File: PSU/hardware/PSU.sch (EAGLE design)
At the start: 203 parts, among them J1 SWD, J2 UART, Q1 PMOS-DPAK, Q10 PMOS-SOT23, Q11 NPN, Q12 PMOS-SOT23, Q2 PMOS-SOT23, Q3 NPN, Q4 PMOS-SOT23, Q5 NMOS-SOT23, Q6 PMOS-DPAK, Q7 PMOS-SOT23, Q8 NMOS-SOT23, Q9 PMOS-DPAK, U1 LM2576, U10 4069, U11 LTV-247, U12 74HC08, U13 STM8S003K3T6C, U14 74HC08, U15 4051, U16 358, U17 358, U18 74HC32, U2 MT3608, U3 7805, U4 324, U5 MC34063, U6 MT3608, U7 LM2576, U8 MC34063, U9 TP4056

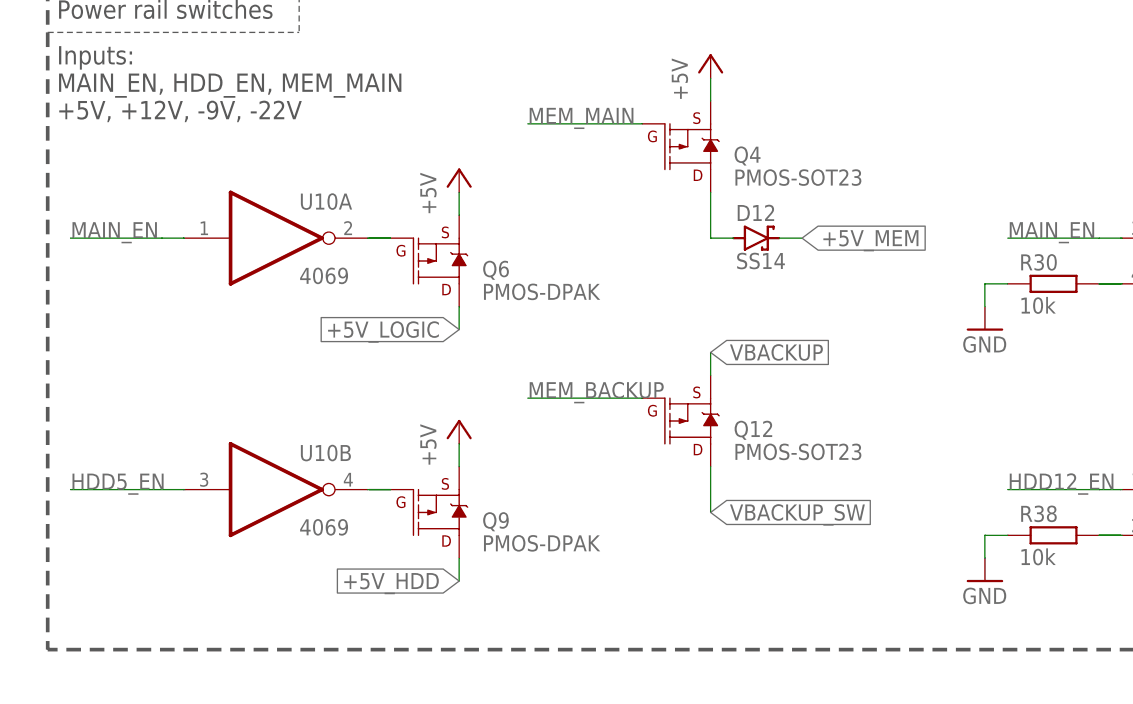
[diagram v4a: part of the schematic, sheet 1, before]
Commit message: [HW/PSU] Fix backup regulator enabling logic level
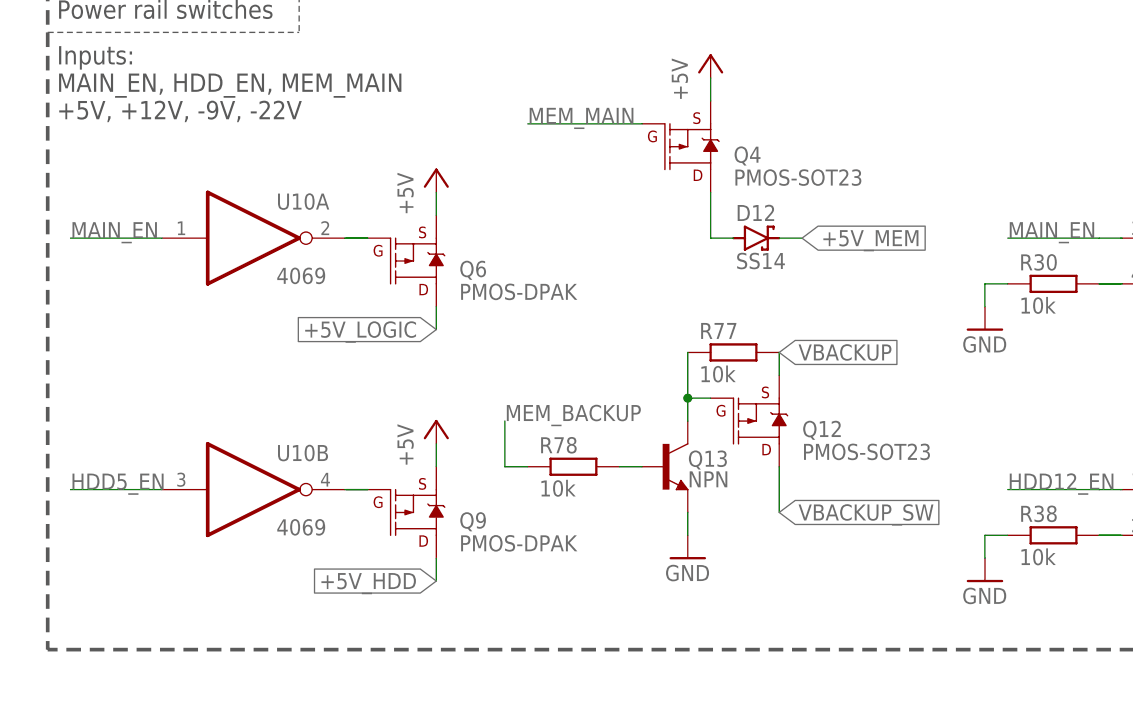
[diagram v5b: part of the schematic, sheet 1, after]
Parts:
- added Q13: NPN, SparkFun-DiscreteSemi:TRANS_NPN-MMBT2222AL
- added R77, R78: 10k, rcl:R-EU_R0805
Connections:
- new net VBACKUP_SW_B: Q13.B, R78.2
- new net VBACKUP_SW_G: Q12.G, Q13.C, R77.1
- net GND: now also Q13.E
- net MEM_BACKUP: now also R78.1; no longer Q12.G
- net VBACKUP: now also R77.2
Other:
- moved on the sheet: Q12, Q6, Q9, U10A, U10B

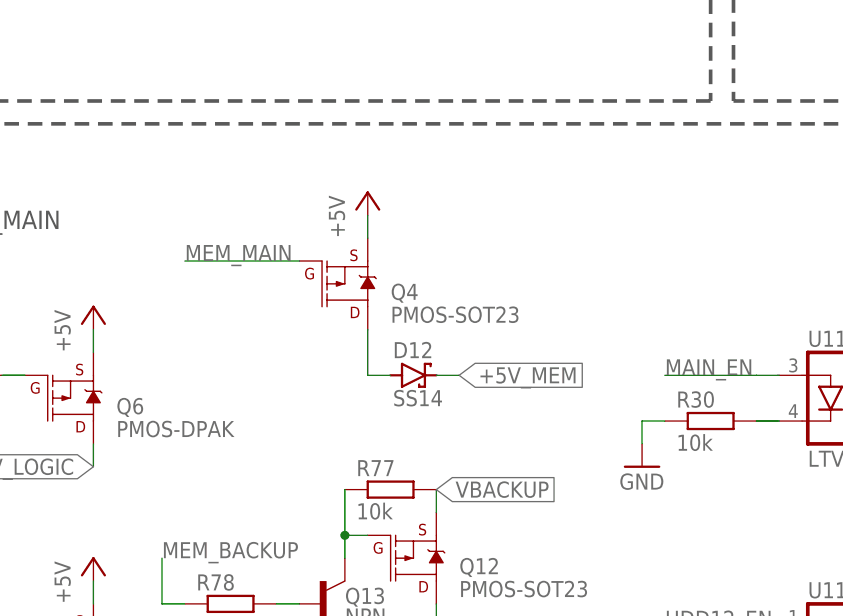
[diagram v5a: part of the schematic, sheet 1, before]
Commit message: [HW/PSU] Fix +5V_MEM enabling logic level
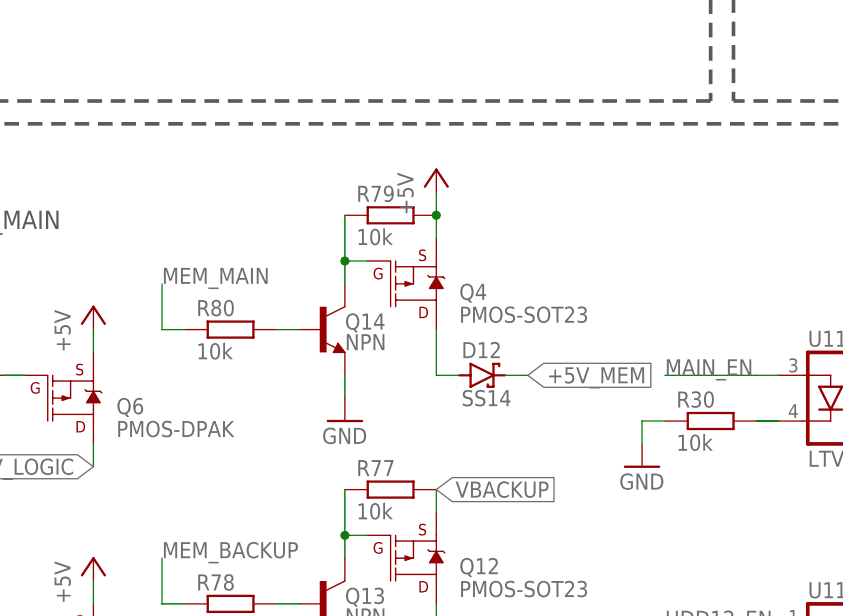
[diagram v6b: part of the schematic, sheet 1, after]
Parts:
- added Q14: NPN, SparkFun-DiscreteSemi:TRANS_NPN-MMBT2222AL
- added R79, R80: 10k, rcl:R-EU_R0805
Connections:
- new net +5VMEM_B: Q14.B, R80.2
- new net +5VMEM_G: Q14.C, Q4.G, R79.1
- net +5V: now also R79.2
- net GND: now also Q14.E
- net MEM_MAIN: now also R80.1; no longer Q4.G
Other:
- moved on the sheet: D12, Q4
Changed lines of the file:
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@@
 <part name="R77" library="rcl" library_urn="urn:adsk.eagle:library:334" deviceset="R-EU_" device="R0805" package3d_urn="urn:adsk.eagle:package:23553/2" value="10k"/>
 <part name="R78" library="rcl" library_urn="urn:adsk.eagle:library:334" deviceset="R-EU_" device="R0805" package3d_urn="urn:adsk.eagle:package:23553/2" value="10k"/>
+<part name="Q14" library="SparkFun-DiscreteSemi" deviceset="TRANS_NPN" device="-MMBT2222AL" value="NPN"/>
+<part name="R80" library="rcl" library_urn="urn:adsk.eagle:library:334" deviceset="R-EU_" device="R0805" package3d_urn="urn:adsk.eagle:package:23553/2" value="10k"/>
+<part name="R79" library="rcl" library_urn="urn:adsk.eagle:library:334" deviceset="R-EU_" device="R0805" package3d_urn="urn:adsk.eagle:package:23553/2" value="10k"/>
+<part name="GND2" library="supply1" library_urn="urn:adsk.eagle:library:371" deviceset="GND" device=""/>
 </parts>
 <sheets>
@@
 <attribute name="VALUE" x="315.722" y="90.17" size="1.778" layer="96" rot="R90"/>
 </instance>
-<instance part="P+22" gate="1" x="81.28" y="73.66" smashed="yes">
-<attribute name="VALUE" x="78.74" y="68.58" size="1.778" layer="96" rot="R90"/>
-</instance>
-<instance part="Q4" gate="G$1" x="78.74" y="63.5" smashed="yes" rot="MR180">
-<attribute name="NAME" x="83.82" y="63.5" size="1.778" layer="95" font="vector" rot="MR180"/>
-<attribute name="VALUE" x="83.82" y="60.96" size="1.778" layer="96" font="vector" rot="MR180"/>
-</instance>
-<instance part="D12" gate="G$1" x="86.36" y="53.34" smashed="yes">
-<attribute name="NAME" x="84.074" y="55.245" size="1.778" layer="95"/>
-<attribute name="VALUE" x="84.074" y="49.911" size="1.778" layer="96"/>
+<instance part="P+22" gate="1" x="88.9" y="76.2" smashed="yes">
+<attribute name="VALUE" x="86.36" y="71.12" size="1.778" layer="96" rot="R90"/>
+</instance>
+<instance part="Q4" gate="G$1" x="86.36" y="63.5" smashed="yes" rot="MR180">
+<attribute name="NAME" x="91.44" y="63.5" size="1.778" layer="95" font="vector" rot="MR180"/>
+<attribute name="VALUE" x="91.44" y="60.96" size="1.778" layer="96" font="vector" rot="MR180"/>
+</instance>
+<instance part="D12" gate="G$1" x="93.98" y="53.34" smashed="yes">
+<attribute name="NAME" x="91.694" y="55.245" size="1.778" layer="95"/>
+<attribute name="VALUE" x="91.694" y="49.911" size="1.778" layer="96"/>
 </instance>
 <instance part="Q1" gate="G$1" x="152.4" y="231.14" smashed="yes">
@@
 <attribute name="NAME" x="62.23" y="29.4386" size="1.778" layer="95"/>
 <attribute name="VALUE" x="62.23" y="24.638" size="1.778" layer="96"/>
+</instance>
+<instance part="Q14" gate="G$1" x="76.2" y="58.42" smashed="yes">
+<attribute name="NAME" x="78.74" y="58.42" size="1.778" layer="95" font="vector"/>
+<attribute name="VALUE" x="78.74" y="56.134" size="1.778" layer="96" font="vector"/>
+</instance>
+<instance part="R80" gate="G$1" x="66.04" y="58.42" smashed="yes">
+<attribute name="NAME" x="62.23" y="59.9186" size="1.778" layer="95"/>
+<attribute name="VALUE" x="62.23" y="55.118" size="1.778" layer="96"/>
+</instance>
+<instance part="R79" gate="G$1" x="83.82" y="71.12" smashed="yes">
+<attribute name="NAME" x="80.01" y="72.6186" size="1.778" layer="95"/>
+<attribute name="VALUE" x="80.01" y="67.818" size="1.778" layer="96"/>
+</instance>
+<instance part="GND2" gate="1" x="78.74" y="48.26" smashed="yes">
+<attribute name="VALUE" x="76.2" y="45.72" size="1.778" layer="96"/>
 </instance>
 </instances>
@@
 <wire x1="78.74" y1="22.86" x2="78.74" y2="20.32" width="0.1524" layer="91"/>
 <pinref part="GND1" gate="1" pin="GND"/>
+</segment>
+<segment>
+<pinref part="Q14" gate="G$1" pin="E"/>
+<wire x1="78.74" y1="53.34" x2="78.74" y2="50.8" width="0.1524" layer="91"/>
+<pinref part="GND2" gate="1" pin="GND"/>
 </segment>
 </net>
@@
 <segment>
 <pinref part="D12" gate="G$1" pin="C"/>
-<wire x1="88.9" y1="53.34" x2="91.44" y2="53.34" width="0.1524" layer="91"/>
-<label x="91.44" y="53.34" size="1.778" layer="95" xref="yes"/>
+<wire x1="96.52" y1="53.34" x2="99.06" y2="53.34" width="0.1524" layer="91"/>
+<label x="99.06" y="53.34" size="1.778" layer="95" xref="yes"/>
 </segment>
 </net>
@@
 <segment>
 <pinref part="Q4" gate="G$1" pin="S"/>
-<wire x1="81.28" y1="68.58" x2="81.28" y2="71.12" width="0.1524" layer="91"/>
+<wire x1="88.9" y1="68.58" x2="88.9" y2="71.12" width="0.1524" layer="91"/>
 <pinref part="P+22" gate="1" pin="+5V"/>
+<pinref part="R79" gate="G$1" pin="2"/>
+<junction x="88.9" y="71.12"/>
+<wire x1="88.9" y1="71.12" x2="88.9" y2="73.66" width="0.1524" layer="91"/>
 </segment>
 </net>
@@
 <net name="MEM_MAIN" class="1">
 <segment>
-<pinref part="Q4" gate="G$1" pin="G"/>
-<wire x1="73.66" y1="66.04" x2="60.96" y2="66.04" width="0.1524" layer="91"/>
-<label x="60.96" y="66.04" size="1.778" layer="95"/>
+<pinref part="R80" gate="G$1" pin="1"/>
+<wire x1="60.96" y1="58.42" x2="58.42" y2="58.42" width="0.1524" layer="91"/>
+<wire x1="58.42" y1="58.42" x2="58.42" y2="63.5" width="0.1524" layer="91"/>
+<label x="58.42" y="63.5" size="1.778" layer="95"/>
 </segment>
 </net>
@@
 <segment>
 <pinref part="Q4" gate="G$1" pin="D"/>
-<wire x1="81.28" y1="58.42" x2="81.28" y2="53.34" width="0.1524" layer="91"/>
+<wire x1="88.9" y1="58.42" x2="88.9" y2="53.34" width="0.1524" layer="91"/>
 <pinref part="D12" gate="G$1" pin="A"/>
-<wire x1="81.28" y1="53.34" x2="83.82" y2="53.34" width="0.1524" layer="91"/>
+<wire x1="88.9" y1="53.34" x2="91.44" y2="53.34" width="0.1524" layer="91"/>
 </segment>
 </net>
@@
 </segment>
 </net>
+<net name="+5VMEM_B" class="1">
+<segment>
+<pinref part="Q14" gate="G$1" pin="B"/>
+<wire x1="73.66" y1="58.42" x2="71.12" y2="58.42" width="0.1524" layer="91"/>
+<pinref part="R80" gate="G$1" pin="2"/>
+</segment>
+</net>
+<net name="+5VMEM_G" class="1">
+<segment>
+<pinref part="Q14" gate="G$1" pin="C"/>
+<wire x1="78.74" y1="63.5" x2="78.74" y2="66.04" width="0.1524" layer="91"/>
+<pinref part="Q4" gate="G$1" pin="G"/>
+<wire x1="78.74" y1="66.04" x2="81.28" y2="66.04" width="0.1524" layer="91"/>
+<wire x1="78.74" y1="66.04" x2="78.74" y2="71.12" width="0.1524" layer="91"/>
+<pinref part="R79" gate="G$1" pin="1"/>
+<junction x="78.74" y="66.04"/>
+</segment>
+</net>

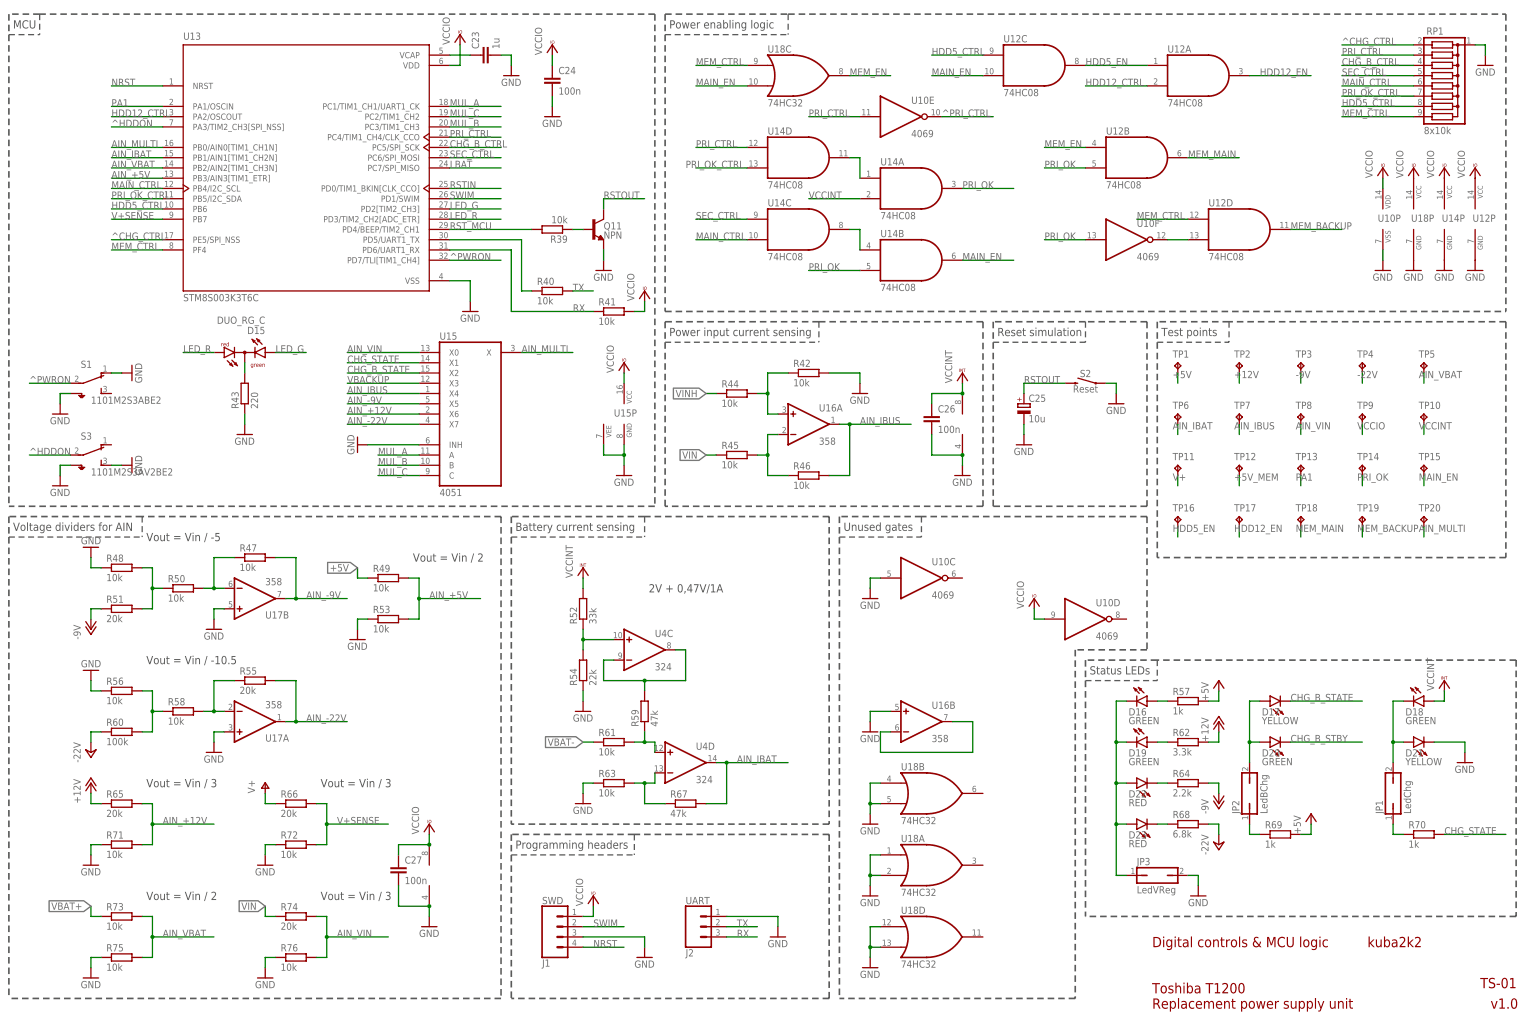
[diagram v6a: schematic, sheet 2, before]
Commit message: [HW/PSU] Fix open-drain GPIO usage
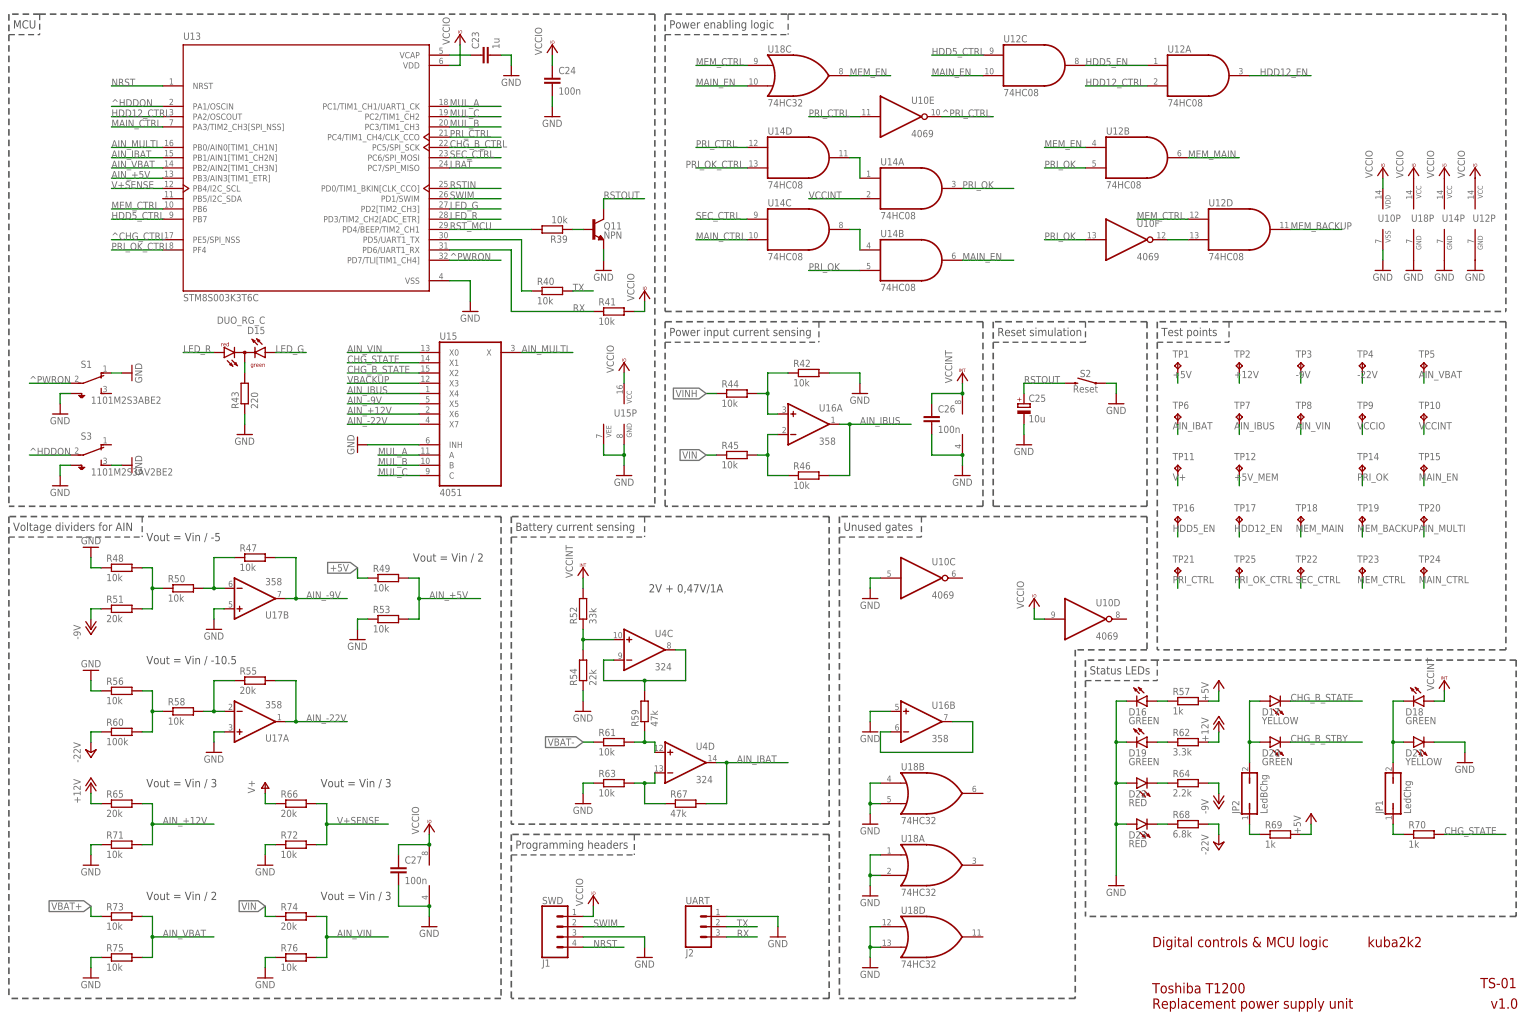
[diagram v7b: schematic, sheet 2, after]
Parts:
- removed JP3: LedVReg, jumper:JP1Q
- removed RP1: 8x10k, custom:RN1X8
- removed TP13: TPB1,27, testpad:TPB1,27
- added TP21, TP22, TP23, TP24, TP25: TPB1,27, testpad:TPB1,27
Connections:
- removed net LED1_EN: D16.C, D19.C, D22.A, D23.A, JP3.1
- removed net PA1: TP13.TP, U13.PA1/OSCIN
- net CHG_B_CTRL: no longer RP1.3
- net GND: now also D16.C, D19.C, D22.A, D23.A; no longer JP3.2, RP1.C
- net HDD5_CTRL: now also U13.PB7; no longer RP1.7, U13.PB6
- net MAIN_CTRL: now also TP24.TP, U13.PA3/TIM2_CH3[SPI_NSS]; no longer RP1.5, U13.PB4/I2C_SCL
- net MEM_CTRL: now also TP23.TP, U13.PB6; no longer RP1.8, U13.PF4
- net PRI_CTRL: now also TP21.TP; no longer RP1.2
- net PRI_OK_CTRL: now also TP25.TP, U13.PF4; no longer RP1.6, U13.PB5/I2C_SDA
- net SEC_CTRL: now also TP22.TP; no longer RP1.4
- net V+SENSE: now also U13.PB4/I2C_SCL; no longer U13.PB7
- net ^CHG_CTRL: no longer RP1.1
- net ^HDDON: now also U13.PA1/OSCIN; no longer U13.PA3/TIM2_CH3[SPI_NSS]

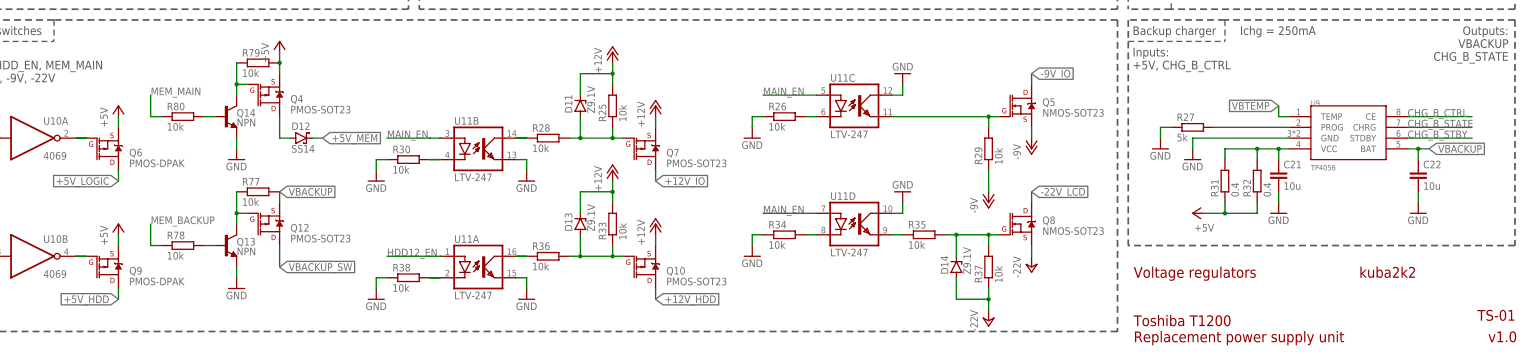
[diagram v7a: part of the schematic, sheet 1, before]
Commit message: [HW/PSU] Fix backup charger enabling, remove standby LEDs
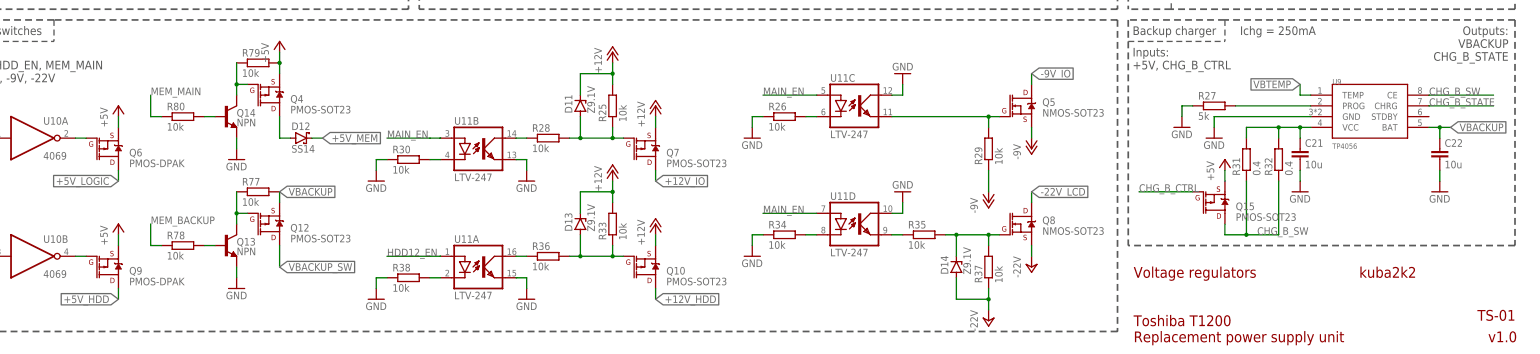
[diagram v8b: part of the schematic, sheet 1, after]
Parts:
- removed D18, D20: GREEN, led:LEDCHIP-LED0805
- added Q15: PMOS-SOT23, SparkFun-DiscreteSemi:MOSFET_PCH-IRLML2244
- added R81: 10k, rcl:R-EU_R0805
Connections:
- removed net CHG_B_STBY: D20.C, U9.STDBY
- new net CHG_B_SW: Q15.D, R31.1, R32.1, U9.CE
- net +5V: now also Q15.S, R81.2; no longer R31.1, R32.1
- net CHG_B_CTRL: now also Q15.G; no longer U9.CE
- net CHG_B_STATE: now also R81.1
- net LED2_EN: no longer D20.A
- net LED3_EN: no longer D18.C
- net VCCINT: no longer D18.A
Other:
- moved on the sheet: C21, C22, R27, R31, R32, U9
